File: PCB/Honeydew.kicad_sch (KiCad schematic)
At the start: 6 parts, among them J9 RGB_EX

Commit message: Large update.
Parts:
- removed A2: QMK Logo, Honeydew:QMK Logo, symbol Mechanical:Fiducial
- removed J9: RGB_EX, Honeydew:PinHeader_1x04_P2.54mm_Vertical_SIlkless, symbol Connector_Generic:Conn_01x04
- added H1: M3, Honeydew:MountingHole_3.2mm_M3_Pad, symbol Mechanical:MountingHole_Pad
- added H2 (x6): M3, Honeydew:MountingHole_3.2mm_M3_Pad, symbol Mechanical:MountingHole
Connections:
- net GND: now also H1.1
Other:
- removed sheet Expansion
- removed sheet USB
- added sheet Comms - SPI (Comms-SPI.kicad_sch)
- added sheet Comms - Split (Comms - Split.kicad_sch)
- added sheet Comms - USB (Comms-USB.kicad_sch)
- sheet MCU ports: added COLM; removed COL12
- sheet Matrix ports: added COLM; removed COL12
- sheet PSU ports: added CC1, CC2; removed none
- sheet RGB ports: added none; removed RGB_EX
- moved on the sheet: A1, H1, H2, H3

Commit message: Added large caps to output of TPS2557. Updated STEP file and file data.
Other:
- sheet Comms - SPI: file Comms-SPI.kicad_sch -> Comms - SPI.kicad_sch
- sheet Comms - USB: file Comms-USB.kicad_sch -> Comms - USB.kicad_sch
- company: (none) -> Created by Ariamelon (https://github.com/Ariamelon/Honeydew/)
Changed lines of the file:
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@@
 (kicad_sch (version 20230121) (generator eeschema)
-  (paper "A5")
+  (paper "A4")
   (title_block
     (title "Honeydew unified split ergonomic keyboard")
-    (date "2023-04-03")
+    (date "2023-04-08")
     (rev "V2.0")
+    (company "Created by Ariamelon (https://github.com/Ariamelon/Honeydew/)")
     (comment 1 "All capacitors 50V unless otherwise specified.")
+    (comment 2 "Licensed under CC BY 4.0.")
   )
   (wire (pts (xy 59.69 49.53) (xy 64.77 49.53))
@@
       (effects (font (size 1.27 1.27)) (justify left bottom))
     )
-    (property "Sheetfile" "Comms-SPI.kicad_sch" (at 39.37 67.8946 0)
+    (property "Sheetfile" "Comms - SPI.kicad_sch" (at 39.37 67.8946 0)
       (effects (font (size 1.27 1.27)) (justify left top) hide)
     )
@@
       (effects (font (size 1.27 1.27)) (justify left bottom))
     )
-    (property "Sheetfile" "Comms-USB.kicad_sch" (at 39.37 24.7146 0)
+    (property "Sheetfile" "Comms - USB.kicad_sch" (at 39.37 24.7146 0)
       (effects (font (size 1.27 1.27)) (justify left top) hide)
     )

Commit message: Shrunk size of PCB.
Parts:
- removed H2 (x2): M3, Honeydew:MountingHole_3.2mm_M3_Pad, symbol Mechanical:MountingHole
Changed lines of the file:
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@@
-    )
-  )
-  (symbol (lib_id "Mechanical:MountingHole") (at 121.92 76.2 0) (mirror y) (unit 1)
-    (in_bom no) (on_board yes) (dnp no)
-    (property "Reference" "H2" (at 124.46 74.93 0)
-      (effects (font (size 1.27 1.27)) (justify right))
-    )
-    (property "Value" "M3" (at 124.46 77.47 0)
-      (effects (font (size 1.27 1.27)) (justify right))
-    )
-    (property "Footprint" "Honeydew:MountingHole_3.2mm_M3_Pad" (at 121.92 76.2 0)
-      (effects (font (size 1.27 1.27)) hide)
-    )
-    (property "Datasheet" "" (at 121.92 76.2 0)
-      (effects (font (size 1.27 1.27)) hide)
-    )
-    (instances
-      (project "Casaba"
-        (path "/24378b90-16c2-4770-828b-ef30a4dde4ac"
-          (reference "H2") (unit 1)
-        )
-      )
-      (project "Honeydew"
-        (path "/534caec7-cf60-4f90-b1ed-42c9d445ef0f"
-          (reference "H10") (unit 1)
-        )
-      )
     )
   )
@@
         )
       )
-    )
-  )
-  (symbol (lib_id "Mechanical:MountingHole") (at 121.92 71.12 0) (mirror y) (unit 1)
-    (in_bom no) (on_board yes) (dnp no)
-    (property "Reference" "H2" (at 124.46 69.85 0)
-      (effects (font (size 1.27 1.27)) (justify right))
-    )
-    (property "Value" "M3" (at 124.46 72.39 0)
-      (effects (font (size 1.27 1.27)) (justify right))
-    )
-    (property "Footprint" "Honeydew:MountingHole_3.2mm_M3_Pad" (at 121.92 71.12 0)
-      (effects (font (size 1.27 1.27)) hide)
-    )
-    (property "Datasheet" "" (at 121.92 71.12 0)
-      (effects (font (size 1.27 1.27)) hide)
-    )
-    (instances
-      (project "Casaba"
-        (path "/24378b90-16c2-4770-828b-ef30a4dde4ac"
-          (reference "H2") (unit 1)
-        )
-      )
-      (project "Honeydew"
-        (path "/534caec7-cf60-4f90-b1ed-42c9d445ef0f"
-          (reference "H9") (unit 1)
-        )
-      )

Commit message: Added plate DXF and gerbers. Removed split comms ports and ideal diode.
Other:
- removed sheet Comms - Split
- sheet MCU ports: added none; removed RX, TX
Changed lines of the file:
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@@
-    (stroke (width 0) (type default))
-  )
-  (wire (pts (xy 59.69 34.29) (xy 64.77 34.29))
     (stroke (width 0) (type default))
   )
@@
   )
   (wire (pts (xy 85.09 46.99) (xy 90.17 46.99))
-    (stroke (width 0) (type default))
-  )
-  (wire (pts (xy 59.69 36.83) (xy 64.77 36.83))
     (stroke (width 0) (type default))
   )
@@
     )
   )
-  (sheet (at 39.37 31.75) (size 20.32 7.62) (fields_autoplaced)
-    (stroke (width 0.1524) (type solid))
-    (fill (color 0 0 0 0.0000))
-    (property "Sheetname" "Comms - Split" (at 39.37 31.0384 0)
-      (effects (font (size 1.27 1.27)) (justify left bottom))
-    )
-    (property "Sheetfile" "Comms - Split.kicad_sch" (at 39.37 39.9546 0)
-      (effects (font (size 1.27 1.27)) (justify left top) hide)
-    )
-    (pin "TX" input (at 59.69 34.29 0)
-      (effects (font (size 1.27 1.27)) (justify right))
-    )
-    (pin "RX" output (at 59.69 36.83 0)
-      (effects (font (size 1.27 1.27)) (justify right))
-    )
-    (instances
-      (project "Honeydew"
-        (path "/534caec7-cf60-4f90-b1ed-42c9d445ef0f" (page "7"))
-      )
-    )
-  )
   (sheet (at 39.37 44.45) (size 20.32 22.86) (fields_autoplaced)
     (stroke (width 0.1524) (type solid))
@@
       (effects (font (size 1.27 1.27)) (justify right))
     )
-    (pin "RX" input (at 64.77 36.83 180)
-      (effects (font (size 1.27 1.27)) (justify left))
-    )
-    (pin "TX" output (at 64.77 34.29 180)
-      (effects (font (size 1.27 1.27)) (justify left))
-    )
     (pin "COLM" output (at 85.09 49.53 0)

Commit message: 17/04/2023 large update.
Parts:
- added H2 (x3): M3, Honeydew:MountingHole_3.2mm_M3_Pad, symbol Mechanical:MountingHole
- A1: footprint Honeydew:Ariamelon_Logo_x3_CU -> Honeydew:Ariamelon_Logo_x3
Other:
- sheet Comms - SPI renamed SPI
- removed sheet Comms - USB
- sheet MCU ports: added 1500mA_EN, 3000mA_EN, ILIM_~{FLT}, I_SEN, MATRIX_CS, OLED_CS, OLED_DC, TB_CS, TB_MOT, TUSB_OUT1, TUSB_OUT2; removed COL0, COL1, COL10, COL11, COL2, COL3, COL4, COL5, COL6, COL7, COL8, COL9, COLM, DC_OLED, MOTION, ROTC, SS_OLED, SS_TB
- sheet Matrix ports: added MATRIX_CS, MOSI, SCK; removed COL0, COL1, COL10, COL11, COL2, COL3, COL4, COL5, COL6, COL7, COL8, COL9, COLM, ROTC
- sheet PSU ports: added 1500mA_EN, 3000mA_EN, D+, D-, ILIM_~{FLT}, I_SEN, TUSB_OUT1, TUSB_OUT2; removed CC1, CC2
- sheet SPI: file Comms - SPI.kicad_sch -> SPI.kicad_sch
- sheet SPI ports: added OLED_CS, OLED_DC, TB_CS, TB_MOT; removed DC_OLED, MOTION, SS_OLED, SS_TB
- moved on the sheet: A1, H1, H2, H3

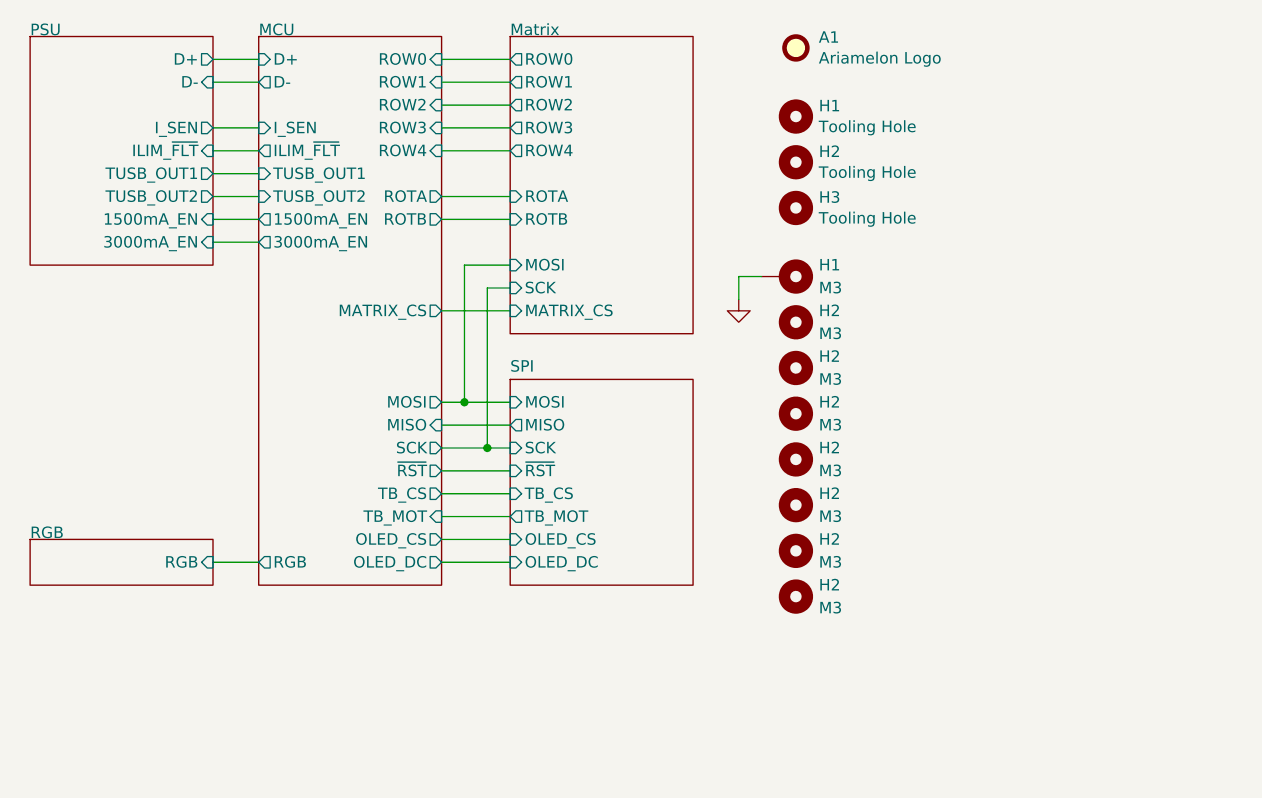
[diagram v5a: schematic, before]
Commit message: 3/4-done update.
Added current and voltage measurement for VBUS in and current measurement for the RGB output. Added PMOS power switch to fully turn off RGB LEDs when not in use. Rerouted the PCB. Moved OLED ribbon cable cutout and expanded it length-wise. Changed position of various components for better routing. Changed bulk capacitance of RGB LEDs to 5 x 22u capacitors. Changed the four N mosfets to two much smaller dual N mosfets. Still need to do RGB routing!
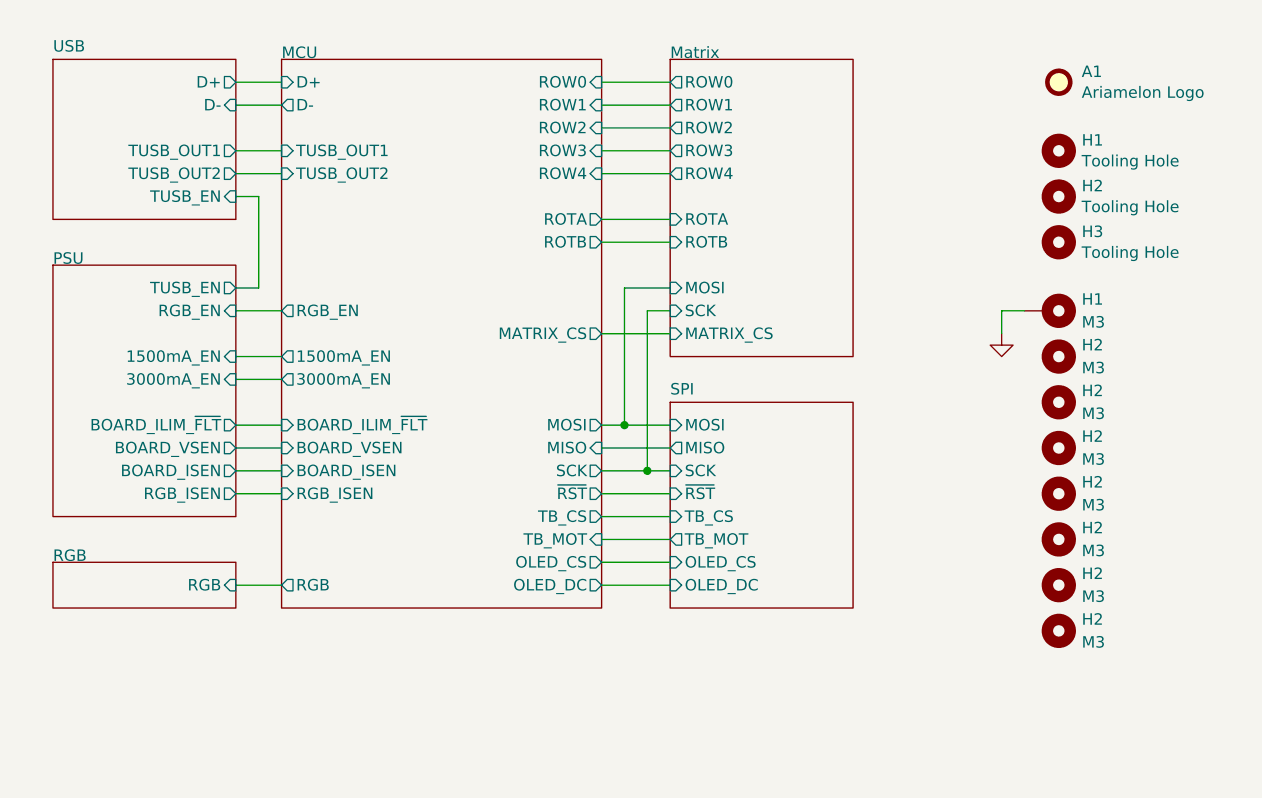
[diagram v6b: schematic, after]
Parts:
- A1: footprint Honeydew:Ariamelon_Logo_x3 -> Honeydew:Ariamelon_Logo_x3_CU
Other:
- added sheet USB (USB.kicad_sch)
- sheet MCU ports: added BOARD_ILIM_~{FLT}, BOARD_ISEN, BOARD_VSEN, RGB_EN, RGB_ISEN; removed ILIM_~{FLT}, I_SEN
- sheet PSU ports: added BOARD_ILIM_~{FLT}, BOARD_ISEN, BOARD_VSEN, RGB_EN, RGB_ISEN, TUSB_EN; removed D+, D-, ILIM_~{FLT}, I_SEN, TUSB_OUT1, TUSB_OUT2
- moved on the sheet: A1, H1, H2, H3

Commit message: 05/05/2023 update.
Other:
- sheet MCU ports: added 1.5A_EN, 3A_EN, RGB_ILIM_~{FLT}; removed 1500mA_EN, 3000mA_EN, RGB_ISEN
- sheet PSU ports: added 1.5A_EN, 3A_EN, RGB_ILIM_~{FLT}; removed 1500mA_EN, 3000mA_EN, RGB_ISEN, TUSB_EN
- sheet USB ports: added none; removed TUSB_EN
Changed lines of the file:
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@@
     (stroke (width 0) (type default))
   )
-  (wire (pts (xy 38.1 58.42) (xy 43.18 58.42))
+  (wire (pts (xy 38.1 60.96) (xy 43.18 60.96))
     (stroke (width 0) (type default))
   )
@@
     (stroke (width 0) (type default))
   )
-  (wire (pts (xy 40.64 43.18) (xy 40.64 33.02))
-    (stroke (width 0) (type default))
-  )
   (wire (pts (xy 86.36 76.2) (xy 78.74 76.2))
     (stroke (width 0) (type default))
@@
     (stroke (width 0) (type default))
   )
+  (wire (pts (xy 43.18 40.64) (xy 38.1 40.64))
+    (stroke (width 0) (type default))
+  )
+  (wire (pts (xy 86.36 43.18) (xy 81.28 43.18))
+    (stroke (width 0) (type default))
+  )
+  (wire (pts (xy 86.36 25.4) (xy 78.74 25.4))
+    (stroke (width 0) (type default))
+  )
+  (wire (pts (xy 43.18 20.32) (xy 38.1 20.32))
+    (stroke (width 0) (type default))
+  )
+  (wire (pts (xy 81.28 58.42) (xy 78.74 58.42))
+    (stroke (width 0) (type default))
+  )
+  (wire (pts (xy 43.18 27.94) (xy 38.1 27.94))
+    (stroke (width 0) (type default))
+  )
+  (wire (pts (xy 86.36 48.26) (xy 78.74 48.26))
+    (stroke (width 0) (type default))
+  )
+  (wire (pts (xy 86.36 20.32) (xy 78.74 20.32))
+    (stroke (width 0) (type default))
+  )
+  (wire (pts (xy 38.1 48.26) (xy 43.18 48.26))
+    (stroke (width 0) (type default))
+  )
   (wire (pts (xy 43.18 45.72) (xy 38.1 45.72))
     (stroke (width 0) (type default))
   )
-  (wire (pts (xy 86.36 43.18) (xy 81.28 43.18))
-    (stroke (width 0) (type default))
-  )
-  (wire (pts (xy 86.36 25.4) (xy 78.74 25.4))
-    (stroke (width 0) (type default))
-  )
-  (wire (pts (xy 43.18 20.32) (xy 38.1 20.32))
-    (stroke (width 0) (type default))
-  )
-  (wire (pts (xy 81.28 58.42) (xy 78.74 58.42))
-    (stroke (width 0) (type default))
-  )
-  (wire (pts (xy 43.18 27.94) (xy 38.1 27.94))
-    (stroke (width 0) (type default))
-  )
-  (wire (pts (xy 86.36 48.26) (xy 78.74 48.26))
-    (stroke (width 0) (type default))
-  )
-  (wire (pts (xy 86.36 20.32) (xy 78.74 20.32))
-    (stroke (width 0) (type default))
-  )
-  (wire (pts (xy 38.1 53.34) (xy 43.18 53.34))
-    (stroke (width 0) (type default))
-  )
-  (wire (pts (xy 43.18 50.8) (xy 38.1 50.8))
-    (stroke (width 0) (type default))
-  )
   (wire (pts (xy 38.1 22.86) (xy 43.18 22.86))
     (stroke (width 0) (type default))
@@
     (stroke (width 0) (type default))
   )
-  (wire (pts (xy 43.18 60.96) (xy 38.1 60.96))
-    (stroke (width 0) (type default))
-  )
-  (wire (pts (xy 38.1 66.04) (xy 43.18 66.04))
+  (wire (pts (xy 43.18 53.34) (xy 38.1 53.34))
+    (stroke (width 0) (type default))
+  )
+  (wire (pts (xy 38.1 63.5) (xy 43.18 63.5))
     (stroke (width 0) (type default))
   )
@@
     (stroke (width 0) (type default))
   )
-  (wire (pts (xy 40.64 33.02) (xy 38.1 33.02))
-    (stroke (width 0) (type default))
-  )
   (wire (pts (xy 38.1 30.48) (xy 43.18 30.48))
     (stroke (width 0) (type default))
   )
-  (wire (pts (xy 38.1 63.5) (xy 43.18 63.5))
+  (wire (pts (xy 38.1 55.88) (xy 43.18 55.88))
     (stroke (width 0) (type default))
   )
   (wire (pts (xy 86.36 71.12) (xy 78.74 71.12))
-    (stroke (width 0) (type default))
-  )
-  (wire (pts (xy 38.1 43.18) (xy 40.64 43.18))
     (stroke (width 0) (type default))
   )
@@
     )
   )
-  (sheet (at 17.78 17.78) (size 20.32 17.78) (fields_autoplaced)
+  (sheet (at 17.78 17.78) (size 20.32 15.24) (fields_autoplaced)
     (stroke (width 0.1524) (type solid))
     (fill (color 0 0 0 0.0000))
@@
       (effects (font (size 1.27 1.27)) (justify left bottom))
     )
-    (property "Sheetfile" "USB.kicad_sch" (at 17.78 36.1446 0)
+    (property "Sheetfile" "USB.kicad_sch" (at 17.78 33.6046 0)
       (effects (font (size 1.27 1.27)) (justify left top) hide)
     )
@@
       (effects (font (size 1.27 1.27)) (justify right))
     )
-    (pin "TUSB_EN" input (at 38.1 33.02 0)
-      (effects (font (size 1.27 1.27)) (justify right))
-    )
     (instances
       (project "Honeydew"
@@
     )
   )
-  (sheet (at 17.78 40.64) (size 20.32 27.94)
+  (sheet (at 17.78 38.1) (size 20.32 27.94)
     (stroke (width 0.1524) (type solid))
     (fill (color 0 0 0 0.0000))
-    (property "Sheetname" "PSU" (at 17.78 40.64 0)
+    (property "Sheetname" "PSU" (at 17.78 38.1 0)
       (effects (font (size 1.27 1.27)) (justify left bottom))
     )
-    (property "Sheetfile" "PSU.kicad_sch" (at 17.78 36.83 0)
+    (property "Sheetfile" "PSU.kicad_sch" (at 17.78 34.29 0)
       (effects (font (size 1.27 1.27)) (justify left) hide)
     )
-    (pin "BOARD_VSEN" output (at 38.1 60.96 0)
-      (effects (font (size 1.27 1.27)) (justify right))
-    )
-    (pin "BOARD_ILIM_~{FLT}" output (at 38.1 58.42 0)
-      (effects (font (size 1.27 1.27)) (justify right))
-    )
-    (pin "BOARD_ISEN" output (at 38.1 63.5 0)
-      (effects (font (size 1.27 1.27)) (justify right))
-    )
-    (pin "1500mA_EN" input (at 38.1 50.8 0)
-      (effects (font (size 1.27 1.27)) (justify right))
-    )
-    (pin "RGB_EN" input (at 38.1 45.72 0)
-      (effects (font (size 1.27 1.27)) (justify right))
-    )
-    (pin "3000mA_EN" input (at 38.1 53.34 0)
-      (effects (font (size 1.27 1.27)) (justify right))
-    )
-    (pin "RGB_ISEN" output (at 38.1 66.04 0)
-      (effects (font (size 1.27 1.27)) (justify right))
-    )
-    (pin "TUSB_EN" output (at 38.1 43.18 0)
+    (pin "BOARD_VSEN" output (at 38.1 53.34 0)
+      (effects (font (size 1.27 1.27)) (justify right))
+    )
+    (pin "BOARD_ILIM_~{FLT}" output (at 38.1 60.96 0)
+      (effects (font (size 1.27 1.27)) (justify right))
+    )
+    (pin "BOARD_ISEN" output (at 38.1 55.88 0)
+      (effects (font (size 1.27 1.27)) (justify right))
+    )
+    (pin "RGB_EN" input (at 38.1 40.64 0)
+      (effects (font (size 1.27 1.27)) (justify right))
+    )
+    (pin "3A_EN" input (at 38.1 48.26 0)
+      (effects (font (size 1.27 1.27)) (justify right))
+    )
+    (pin "1.5A_EN" input (at 38.1 45.72 0)
+      (effects (font (size 1.27 1.27)) (justify right))
+    )
+    (pin "RGB_ILIM_~{FLT}" output (at 38.1 63.5 0)
       (effects (font (size 1.27 1.27)) (justify right))
     )
@@
       (effects (font (size 1.27 1.27)) (justify right))
     )
-    (pin "3000mA_EN" output (at 43.18 53.34 180)
-      (effects (font (size 1.27 1.27)) (justify left))
-    )
     (pin "TUSB_OUT2" input (at 43.18 30.48 180)
       (effects (font (size 1.27 1.27)) (justify left))
@@
       (effects (font (size 1.27 1.27)) (justify left))
     )
-    (pin "1500mA_EN" output (at 43.18 50.8 180)
-      (effects (font (size 1.27 1.27)) (justify left))
-    )
-    (pin "BOARD_ISEN" input (at 43.18 63.5 180)
-      (effects (font (size 1.27 1.27)) (justify left))
-    )
-    (pin "BOARD_VSEN" input (at 43.18 60.96 180)
-      (effects (font (size 1.27 1.27)) (justify left))
-    )
-    (pin "RGB_ISEN" input (at 43.18 66.04 180)
-      (effects (font (size 1.27 1.27)) (justify left))
-    )
-    (pin "BOARD_ILIM_~{FLT}" input (at 43.18 58.42 180)
-      (effects (font (size 1.27 1.27)) (justify left))
-    )
-    (pin "RGB_EN" output (at 43.18 45.72 180)
-      (effects (font (size 1.27 1.27)) (justify left))
-    )
+    (pin "BOARD_ISEN" input (at 43.18 55.88 180)
+      (effects (font (size 1.27 1.27)) (justify left))
+    )
+    (pin "BOARD_VSEN" input (at 43.18 53.34 180)
+      (effects (font (size 1.27 1.27)) (justify left))
+    )
+    (pin "BOARD_ILIM_~{FLT}" input (at 43.18 60.96 180)
+      (effects (font (size 1.27 1.27)) (justify left))
+    )
+    (pin "RGB_EN" output (at 43.18 40.64 180)
+      (effects (font (size 1.27 1.27)) (justify left))
+    )
+    (pin "3A_EN" output (at 43.18 48.26 180)
+      (effects (font (size 1.27 1.27)) (justify left))
+    )
+    (pin "1.5A_EN" output (at 43.18 45.72 180)
+      (effects (font (size 1.27 1.27)) (justify left))
+    )
+    (pin "RGB_ILIM_~{FLT}" input (at 43.18 63.5 180)
+      (effects (font (size 1.27 1.27)) (justify left))
+    )
